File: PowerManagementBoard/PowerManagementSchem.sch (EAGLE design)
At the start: 6 parts, among them U1 3V3REG, U2 PYB20-Q24-S5, U3 PYB30-Q48-S5, U4 PYB30-Q48-S12, U5 VX7805-500

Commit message: Wired up CUI modules, added blank sheets for other devices
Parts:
- removed B1: TEENSY-3.1SILK, SparkFun-Boards:TEENSY-3.1SILK
- added C1, C3, C8: 10uF, rcl:C-USC1206
- added C10, C6, C7: 0.1uF, rcl:C-USC0805
- added C2, C5, C9: 10uF, rcl:C-USC0805
- added C4: (no value), rcl:C-USC1206
- added J1: D15S24A4GV00LF, D-Sub Connectors:D15S24A4GV00LF
- added R1, R2, R3, R4, R5, R6: DNP, rcl:R-US_R0805
- added TP_12V_CTRL, TP_5V-ACT_CTRL, TP_5V-DIG_CTRL: TPTP15R, testpad:TPTP15R
- U1: value 3V3REG -> VX7805-500; device PowerManagementParts:3V3REG -> CUI_DCDC_Conv:VX7805-500
- U5: value VX7805-500 -> 3V3REG; device CUI_DCDC_Conv:VX7805-500 -> PowerManagementParts:3V3REG
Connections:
- new net 12V: C5.1, C6.1, R2.2, U4.+VO
- new net 5V-ACT: C2.1, C7.1, R4.2, U3.+VO
- new net 5V-DIG: C10.1, C9.1, R6.2, U2.+VO
- new net GND: C1.2, C10.2, C2.2, C3.2, C5.2, C6.2, C7.2, C8.2, C9.2, R1.1, U2.GND, U3.GND, U4.0V, U4.GND
- new net N$1: TP_12V_CTRL.TP, U4.CTRL
- new net N$2: TP_5V-ACT_CTRL.TP, U3.CTRL
- new net N$3: R1.2, R2.1, U4.TRIM
- new net N$4: R3.2, R4.1, U3.TRIM
- new net N$5: R3.1, U3.0V
- new net N$6: TP_5V-DIG_CTRL.TP, U2.CTRL
- new net N$7: R5.2, R6.1, U2.TRIM
- new net N$8: R5.1, U2.0V
- new net SUPPLY_FOR_12V: C3.1, U4.VIN
- new net SUPPLY_FOR_5V-ACT: C1.1, U3.VIN
- new net SUPPLY_FOR_5V-DIG: C8.1, U2.VIN
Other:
- note added: "12V Supply"
- note added: "5V-Act Supply"
- note added: "5V-Dig Supply"

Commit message: Added board file
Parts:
- added C11, C13: 10uF, rcl:C-USC0805
- added C12, C14: 0.1uF, rcl:C-USC0805
- C4: value (none) -> 10uF
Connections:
- new net MNGR-3.3V: C13.1, C14.1, U5.VOUT
- new net MNGR-5V: C11.1, C12.1, U1.+VOUT, U5.INPUT
- new net SUPPLY_FOR_MNGR: C4.1, U1.+VIN
- net GND: now also C11.2, C12.2, C13.2, C14.2, C4.2, U1.GND, U5.GND
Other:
- note added: "Note: Provided connector is likely solder-cup style. Use 3d printed jig to mount to board using bolts and 1 wire per position."
- moved on the sheet: C4, U1, U5

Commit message: Added MOSFET to lib. Added Teensy to schem
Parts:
- added B1: TEENSY-4.0SILK, PowerManagementParts:TEENSY-4.0SILK
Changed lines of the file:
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@@
 <part name="C14" library="rcl" library_urn="urn:adsk.eagle:library:334" deviceset="C-US" device="C0805" package3d_urn="urn:adsk.eagle:package:23617/2" value="0.1uF"/>
 <part name="GND2" library="supply1" library_urn="urn:adsk.eagle:library:371" deviceset="GND" device=""/>
+<part name="B1" library="PowerManagementParts" deviceset="TEENSY-4.0" device="SILK" package3d_urn="urn:adsk.eagle:package:37333/1"/>
+<part name="FRAME2" library="frames" library_urn="urn:adsk.eagle:library:229" deviceset="FRAME_A_L" device=""/>
+<part name="FRAME3" library="frames" library_urn="urn:adsk.eagle:library:229" deviceset="FRAME_A_L" device=""/>
 </parts>
 <sheets>
@@
 &lt;Connections for the Teensy and possible datalogging capability. Do not include op-amps here.&gt;</description>
 <plain>
+<text x="175.26" y="25.4" size="2.54" layer="94">Graham Braly
+Mark Gilliland</text>
+<text x="271.78" y="25.4" size="2.54" layer="94" align="bottom-right">RockSat-X: Mines</text>
 </plain>
 <instances>
+<instance part="B1" gate="G$1" x="40.64" y="55.88" smashed="yes">
+<attribute name="NAME" x="35.56" y="86.614" size="1.778" layer="95" font="vector"/>
+<attribute name="VALUE" x="35.56" y="22.606" size="1.778" layer="96" font="vector" align="top-left"/>
+</instance>
+<instance part="FRAME2" gate="G$1" x="0" y="0" smashed="yes"/>
+<instance part="FRAME2" gate="G$2" x="172.72" y="0" smashed="yes">
+<attribute name="LAST_DATE_TIME" x="185.42" y="1.27" size="2.54" layer="94"/>
+<attribute name="SHEET" x="259.08" y="1.27" size="2.54" layer="94"/>
+<attribute name="DRAWING_NAME" x="190.5" y="19.05" size="2.54" layer="94"/>
+</instance>
 </instances>
 <busses>
@@
 <description>Channel Control and Sense &lt;Current Sense circuits, outputs, and multiplexing&gt;</description>
 <plain>
+<text x="175.26" y="25.4" size="2.54" layer="94">Graham Braly
+Mark Gilliland</text>
+<text x="271.78" y="25.4" size="2.54" layer="94" align="bottom-right">RockSat-X: Mines</text>
 </plain>
 <instances>
+<instance part="FRAME3" gate="G$1" x="0" y="0" smashed="yes"/>
+<instance part="FRAME3" gate="G$2" x="172.72" y="0" smashed="yes">
+<attribute name="LAST_DATE_TIME" x="185.42" y="1.27" size="2.54" layer="94"/>
+<attribute name="SHEET" x="259.08" y="1.27" size="2.54" layer="94"/>
+<attribute name="DRAWING_NAME" x="190.5" y="19.05" size="2.54" layer="94"/>
+</instance>
 </instances>
 <busses>

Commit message: Created control for Laser and TX. Minor teaks to current amp part.
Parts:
- added R10, R11, R12, R13, R14, R7, R8, R9: 0.01Ω, rcl:R-US_R1206
- added RN1, RN3: 100k, PowerManagementParts:4816P-T01-104LF
- added RN2, RN4: 100Ω, PowerManagementParts:4816P-T01-101LF
- added U$1, U$10, U$4, U$5, U$6, U$7, U$8, U$9: PMOSFET, usbMotorDriverParts:PMOSFET
- added U$2, U$3: MOLEX_3PIN, PowerManagementParts:MOLEX_3PIN
- added U6: INA4180-SPLIT, PowerManagementParts:INA4180-SPLIT
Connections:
- new net 5-ACT-LASER-EN: RN2G$4.1
- new net 5V-ACT-LASER: R10.1, U$3.PIN2, U6G4.IN-
- new net 5V-ACT-LASER-SNS: U6G4.OUT
- new net 5V-ACT-TX: R8.1, U$2.PIN2, U6G2.IN-
- new net 5V-ACT-TX-EN: RN2G$2.1
- new net 5V-ACT-TX-SNS: U6G2.OUT
- new net 5V-DIG-LASER: R9.1, U$3.PIN3, U6G3.IN-
- new net 5V-DIG-LASER-EN: RN2G$3.1
- new net 5V-DIG-LASER-SNS: U6G3.OUT
- new net 5V-DIG-TX: R7.1, U$2.PIN3, U6G1.IN-
- new net 5V-DIG-TX-EN: RN2G$1.1
- new net 5V-DIG-TX-SNS: U6G1.OUT
- new net N$10: RN1G$2.1, RN2G$2.2, U$6.G
- new net N$11: R7.2, U$1.D, U6G1.IN+
- new net N$12: R8.2, U$6.D, U6G2.IN+
- new net N$13: RN1G$3.1, RN2G$3.2, U$7.G
- new net N$14: R9.2, U$7.D, U6G3.IN+
- new net N$15: RN1G$4.1, RN2G$4.2, U$8.G
- new net N$16: R10.2, U$8.D, U6G4.IN+
- new net N$17: RN1G$5.1, RN2G$5.2, U$9.G
- new net N$18: R11.2, U$9.D
- new net N$19: RN1G$6.1, RN2G$6.2, U$10.G
- new net N$20: R12.2, U$10.D
- new net N$21: RN3G$5.1, RN4G$5.2, U$4.G
- new net N$22: R13.2, U$4.D
- new net N$23: RN3G$6.1, RN4G$6.2, U$5.G
- new net N$24: R14.2, U$5.D
- new net N$9: RN1G$1.1, RN2G$1.2, U$1.G
- net 5V-DIG: now also RN1G$1.2, U$1.S
- net GND: now also U$2.PIN1, U$3.PIN1, U6G$5.GND
- net MNGR-3.3V: now also U6G$5.V+
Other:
- note added: "5V-ACT"
- note added: "5V-DIG"
- note added: "Laser"
- note added: "Transmitter"

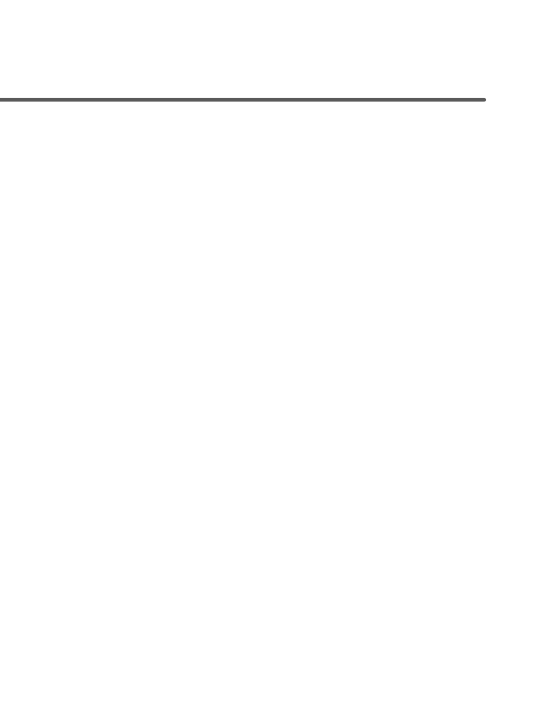
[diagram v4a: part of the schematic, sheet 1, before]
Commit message: Created very rough layout of large parts on board. Added mounting holes.
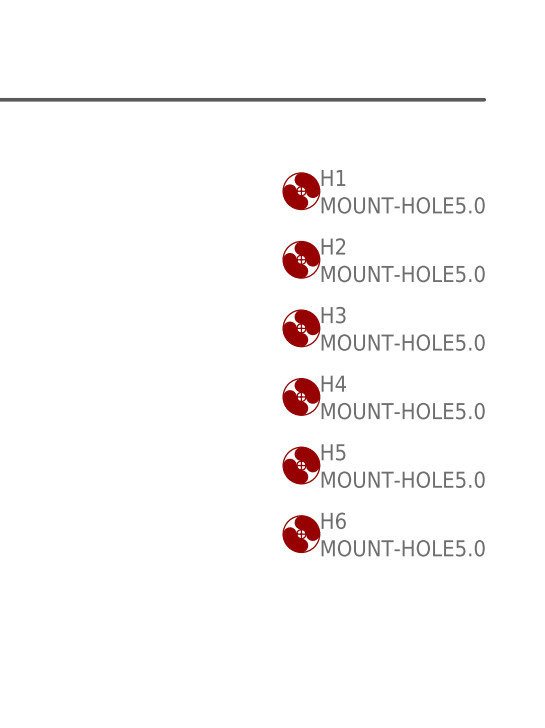
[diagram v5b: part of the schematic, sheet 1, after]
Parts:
- added H1, H2, H3, H4, H5, H6: MOUNT-HOLE5.0, holes:MOUNT-HOLE5.0
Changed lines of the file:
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@@
 <part name="R14" library="rcl" library_urn="urn:adsk.eagle:library:334" deviceset="R-US_" device="R1206" package3d_urn="urn:adsk.eagle:package:23540/2" value="0.01Ω"/>
 <part name="FRAME4" library="frames" library_urn="urn:adsk.eagle:library:229" deviceset="FRAME_A_L" device=""/>
+<part name="H1" library="holes" library_urn="urn:adsk.eagle:library:237" deviceset="MOUNT-HOLE" device="5.0" package3d_urn="urn:adsk.eagle:package:14276/1"/>
+<part name="H2" library="holes" library_urn="urn:adsk.eagle:library:237" deviceset="MOUNT-HOLE" device="5.0" package3d_urn="urn:adsk.eagle:package:14276/1"/>
+<part name="H3" library="holes" library_urn="urn:adsk.eagle:library:237" deviceset="MOUNT-HOLE" device="5.0" package3d_urn="urn:adsk.eagle:package:14276/1"/>
+<part name="H4" library="holes" library_urn="urn:adsk.eagle:library:237" deviceset="MOUNT-HOLE" device="5.0" package3d_urn="urn:adsk.eagle:package:14276/1"/>
+<part name="H5" library="holes" library_urn="urn:adsk.eagle:library:237" deviceset="MOUNT-HOLE" device="5.0" package3d_urn="urn:adsk.eagle:package:14276/1"/>
+<part name="H6" library="holes" library_urn="urn:adsk.eagle:library:237" deviceset="MOUNT-HOLE" device="5.0" package3d_urn="urn:adsk.eagle:package:14276/1"/>
 </parts>
 <sheets>
@@
 <attribute name="VALUE" x="246.38" y="172.72" size="1.778" layer="96"/>
 </instance>
+<instance part="H1" gate="G$1" x="254" y="129.54" smashed="yes">
+<attribute name="NAME" x="256.032" y="130.1242" size="1.778" layer="95"/>
+<attribute name="VALUE" x="256.032" y="127.0762" size="1.778" layer="96"/>
+</instance>
+<instance part="H2" gate="G$1" x="254" y="121.92" smashed="yes">
+<attribute name="NAME" x="256.032" y="122.5042" size="1.778" layer="95"/>
+<attribute name="VALUE" x="256.032" y="119.4562" size="1.778" layer="96"/>
+</instance>
+<instance part="H3" gate="G$1" x="254" y="114.3" smashed="yes">
+<attribute name="NAME" x="256.032" y="114.8842" size="1.778" layer="95"/>
+<attribute name="VALUE" x="256.032" y="111.8362" size="1.778" layer="96"/>
+</instance>
+<instance part="H4" gate="G$1" x="254" y="106.68" smashed="yes">
+<attribute name="NAME" x="256.032" y="107.2642" size="1.778" layer="95"/>
+<attribute name="VALUE" x="256.032" y="104.2162" size="1.778" layer="96"/>
+</instance>
+<instance part="H5" gate="G$1" x="254" y="99.06" smashed="yes">
+<attribute name="NAME" x="256.032" y="99.6442" size="1.778" layer="95"/>
+<attribute name="VALUE" x="256.032" y="96.5962" size="1.778" layer="96"/>
+</instance>
+<instance part="H6" gate="G$1" x="254" y="91.44" smashed="yes">
+<attribute name="NAME" x="256.032" y="92.0242" size="1.778" layer="95"/>
+<attribute name="VALUE" x="256.032" y="88.9762" size="1.778" layer="96"/>
+</instance>
 </instances>

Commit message: Updated some schem sybmols, wired up the MOSFET for cam and static
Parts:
- removed B1: TEENSY-4.0SILK, PowerManagementParts:TEENSY-4.0SILK
- removed RN3: 100k, PowerManagementParts:4816P-T01-104LF
- removed RN4: 100Ω, PowerManagementParts:4816P-T01-101LF
- added R15, R16, R17, R18: 0.01Ω, rcl:R-US_R1206
- added R19: 1.2k, rcl:R-US_R0805
- added U$11, U$12: MOLEX_4PIN, PowerManagementParts:MOLEX_4PIN
- added U$13, U$14, U$15, U$16: PMOSFET, usbMotorDriverParts:PMOSFET
- added U$17: FLAT_LED, PowerManagementParts:FLAT_LED
- added U$18, U$19: CD4051B_ALT, PowerManagementParts:CD4051B_ALT
- added U7: INA4180-SPLIT, PowerManagementParts:INA4180-SPLIT
- added U8: TEENSY-4.0SILK, PowerManagementParts:TEENSY-4.0SILK
- R11, R12: value 0.01Ω -> 330; device rcl:R-US_R1206 -> rcl:R-US_R0805
- U$10, U$9: value PMOSFET -> FLAT_LED; device usbMotorDriverParts:PMOSFET -> PowerManagementParts:FLAT_LED
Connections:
- removed net N$20: R12.2, U$10.D
- new net 12V-CAM: U$11.PIN1
- new net 12V-STA: U$12.PIN1
- new net 5V-ACT-CAM: R17.1, U$11.PIN3, U7G2.IN-
- new net 5V-ACT-CAM-EN: RN2-6.1
- new net 5V-ACT-CAM-SNS: U7G2.OUT
- new net 5V-ACT-LASER-EN: U8.5*
- new net 5V-ACT-STA: R15.1, U$12.PIN3, U7G4.IN-
- new net 5V-ACT-STA-EN: RN2-8.1
- new net 5V-ACT-STA-SNS: U7G4.OUT
- new net 5V-DIG-CAM: R18.1, U$11.PIN4, U7G1.IN-
- new net 5V-DIG-CAM-EN: RN2-5.1
- new net 5V-DIG-CAM-SNS: U7G1.OUT
- new net 5V-DIG-STA: R16.1, U$12.PIN4, U7G3.IN-
- new net 5V-DIG-STA-EN: RN2-7.1
- new net 5V-DIG-STA-SNS: U7G3.OUT
- new net CURRENT-SNS-A: U$18.COMI/O, U8.A8/22*
- new net CURRENT-SNS-B: U$19.COMI/O, U8.A9/23*
- new net N$25: RN1-8.1, RN2-8.2, U$13.G
- new net N$26: R15.2, U$13.D, U7G4.IN+
- new net N$27: RN1-7.1, RN2-7.2, U$14.G
- new net N$28: R16.2, U$14.D, U7G3.IN+
- new net N$29: RN1-6.1, RN2-6.2, U$15.G
- new net N$30: R17.2, U$15.D, U7G2.IN+
- new net N$31: RN1-5.1, RN2-5.2, U$16.G
- new net N$32: R18.2, U$16.D, U7G1.IN+
- new net N$36: U8.6*
- new net N$37: U8.7/RX3
- new net N$38: U8.8/TX3
- new net N$39: U8.9*/RX2
- new net N$40: U8.10*/TX2/CS
- net 12V: now also U$17.ANODE
- net 5-ACT-LASER-EN: now also RN2-4.1; no longer RN2G$4.1
- net 5V-ACT: now also RN1-2.2, RN1-4.2, RN1-6.2, RN1-8.2, U$10.ANODE, U$13.S, U$15.S, U$6.S, U$8.S
- net 5V-ACT-TX-EN: now also RN2-2.1, U8.3*; no longer RN2G$2.1
- net 5V-DIG: now also RN1-1.2, RN1-3.2, RN1-5.2, RN1-7.2, U$14.S, U$16.S, U$7.S, U$9.ANODE; no longer RN1G$1.2
- net 5V-DIG-LASER-EN: now also RN2-3.1, U8.4*; no longer RN2G$3.1
- net 5V-DIG-TX-EN: now also RN2-1.1, U8.2; no longer RN2G$1.1
- net GND: now also R11.1, R12.1, R19.1, U$11.PIN2, U$12.PIN2, U7G$5.GND, U8.GND
- net MNGR-3.3V: now also U7G$5.V+
- net N$10: now also RN1-2.1, RN2-2.2; no longer RN1G$2.1, RN2G$2.2
- net N$13: now also RN1-3.1, RN2-3.2; no longer RN1G$3.1, RN2G$3.2
- net N$15: now also RN1-4.1, RN2-4.2; no longer RN1G$4.1, RN2G$4.2
- net N$17: now also R11.2, U$9.CATHODE; no longer RN1G$5.1, RN2G$5.2, U$9.G
- net N$18: now also R12.2, U$10.CATHODE; no longer R11.2, U$9.D
- net N$19: now also R19.2, U$17.CATHODE; no longer RN1G$6.1, RN2G$6.2, U$10.G
- net N$21: no longer RN3G$5.1, RN4G$5.2
- net N$23: no longer RN3G$6.1, RN4G$6.2
- net N$9: now also RN1-1.1, RN2-1.2; no longer RN1G$1.1, RN2G$1.2
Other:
- note added: "Boom Camera"
- note added: "Static"

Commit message: Added notes and minor changes
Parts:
- added D1, D10, D11, D12, D2, D3, D4, D5, D6, D7, D8, D9: S1M, diode:S1M
- added R20, R21: 0.01Ω, rcl:R-US_R1206
- added R22: 330, rcl:R-US_R0805
- added RN3: 100Ω, PowerManagementParts:4816P-T01-101LF
- added RN4: 100kΩ, PowerManagementParts:4816P-T01-104LF
- added U$20: FLAT_LED, PowerManagementParts:FLAT_LED
- added U$22, U$23: PMOSFET, usbMotorDriverParts:PMOSFET
- added U$24: MOLEX_3PIN, PowerManagementParts:MOLEX_3PIN
- added U9: INA4180-SPLIT, PowerManagementParts:INA4180-SPLIT
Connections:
- net N$38 renamed 12V-CAM-EN
- removed net N$39: U8.9*/RX2
- new net 12V-CAM-SNS: U$18.CH5
- new net 12V-STA-EN: U8.A2/16
- new net 12V-STA-SNS: U$19.CH5
- new net 5V-ACT-MAG: R13.1, U$24.PIN2, U9G2.IN-
- new net 5V-ACT-MAG-EN: RN3-2.1, U8.10*/TX2/CS
- new net 5V-ACT-MAG-SNS: U$19.CH3, U9G2.OUT
- new net 5V-DIG-MAG: R14.1, U$24.PIN3, U9G1.IN-
- new net 5V-DIG-MAG-EN: RN3-1.1, U8.9*/RX2
- new net 5V-DIG-MAG-SNS: U$18.CH3, U9G1.OUT
- new net MUX-SEL-A: U$18.CH_A, U$19.CH_A, U8.A3/17
- new net MUX-SEL-B: U$18.CH_B, U$19.CH_B, U8.A6/20*
- new net MUX-SEL-C: U$18.CH_C, U$19.CH_C, U8.A7/21*
- new net N$20: R22.2, U$20.CATHODE
- new net N$34: R20.2, U$22.D, U9G3.IN+
- new net N$35: R20.1, U9G3.IN-
- new net N$41: RN4-3.2, U$22.S
- new net N$42: RN4-4.2, U$23.S
- new net N$43: RN3-4.2, RN4-4.1, U$23.G
- net 5V-ACT: now also D10.C, D2.C, D4.C, D6.C, D8.C, RN4-2.2, U$4.S
- net 5V-ACT-CAM-EN: now also U8.7/RX3
- net 5V-ACT-CAM-SNS: now also U$19.CH2
- net 5V-ACT-LASER-SNS: now also U$19.CH1
- net 5V-ACT-STA-EN: now also U8.A1/15
- net 5V-ACT-STA-SNS: now also U$19.CH4
- net 5V-ACT-TX-SNS: now also U$19.CH0
- net 5V-DIG: now also D3.C, D5.C, D7.C, D9.C, RN4-1.2, U$5.S
- net 5V-DIG-CAM-EN: now also U8.6*
- net 5V-DIG-CAM-SNS: now also U$18.CH2
- net 5V-DIG-LASER-SNS: now also U$18.CH1
- net 5V-DIG-STA-EN: now also U8.A0/14
- net 5V-DIG-STA-SNS: now also U$18.CH4
- net 5V-DIG-TX-SNS: now also U$18.CH0
- net GND: now also R22.1, U$18.GND, U$18.VEE, U$19.GND, U$19.VEE, U$24.PIN1, U9G$5.GND
- net MNGR-3.3V: now also U$18.VDD, U$19.VDD, U9G$5.V+
- net MNGR-5V: now also U$20.ANODE
- net N$12: now also D2.A
- net N$14: now also D3.A
- net N$16: now also D4.A
- net N$21: now also RN3-2.2, RN4-2.1
- net N$22: now also D10.A, U9G2.IN+
- net N$23: now also RN3-1.2, RN4-1.1
- net N$24: now also D9.A, U9G1.IN+
- net N$26: now also D8.A
- net N$28: now also D7.A
- net N$30: now also D6.A
- net N$32: now also D5.A
- net N$36: now also R21.2, U$23.D, U9G4.IN+; no longer U8.6*
- net N$37: now also R21.1, U9G4.IN-; no longer U8.7/RX3
- net N$40: now also RN3-3.2, RN4-3.1, U$22.G; no longer U8.10*/TX2/CS
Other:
- note added: "12V Control"
- note added: "Magnet Experiment"
- note added: "add connections"
- note added: "add test points"

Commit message: Test: tried changing hole diameter on this branch while other branch is modified
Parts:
- added U$21: FLAT_LED, PowerManagementParts:FLAT_LED
- H1, H2, H3, H4, H5, H6: value MOUNT-HOLE5.0 -> MOUNT-HOLE3.0; device holes:MOUNT-HOLE5.0 -> holes:MOUNT-HOLE3.0
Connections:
- removed net N$41: RN4-3.2, U$22.S
- new net N$33: RN3-3.1
- net 12V: now also RN4-3.2, U$22.S
- net 12V-CAM-SNS: now also U9G3.OUT
- net MNGR-3.3V: now also U8.3.3V
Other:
- note added: "12V-CAM"
- note added: "test for git"
- moved on the sheet: D11, D12, R20, R21, RN3-3, RN3-4, RN4-3, RN4-4, U$22, U$23, U9G3, U9G4
